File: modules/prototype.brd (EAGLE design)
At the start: 117 parts

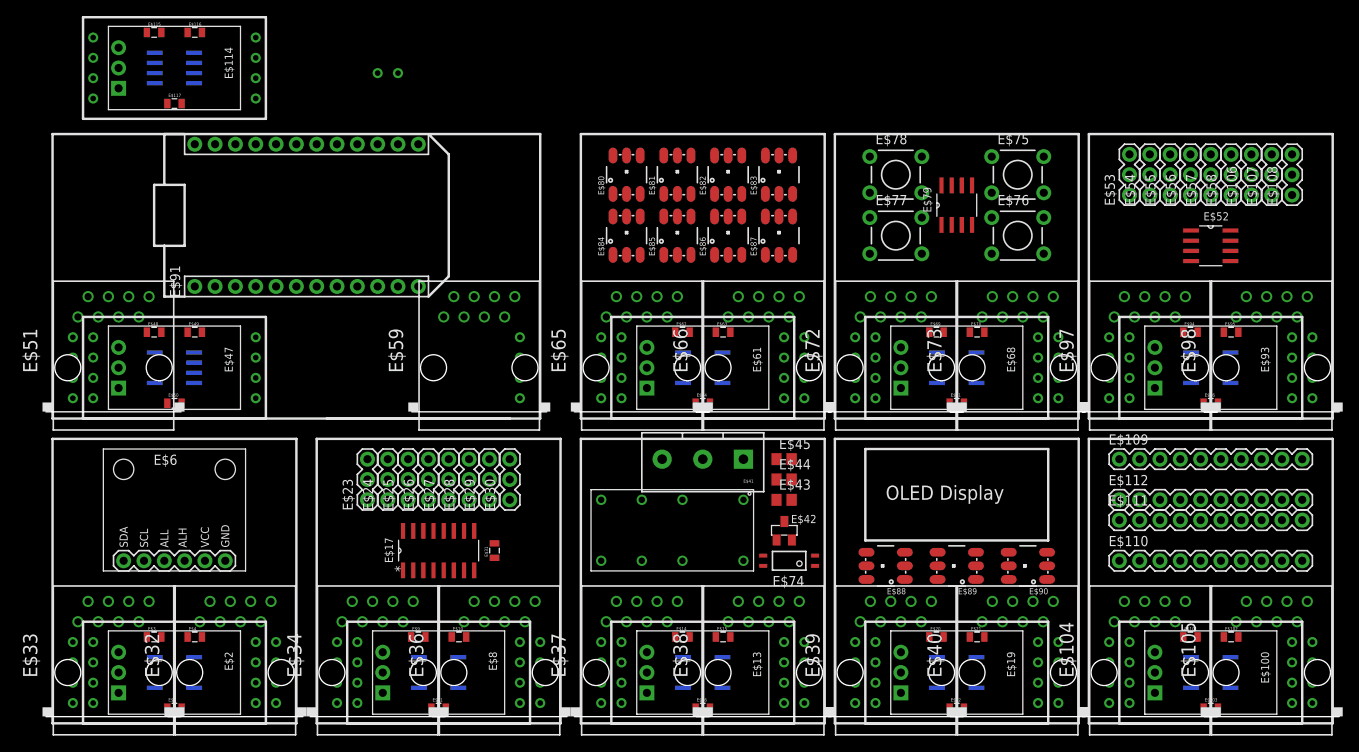
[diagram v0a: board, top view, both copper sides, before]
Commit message: Updates to v1 of reg_i2c. New ext_i2c
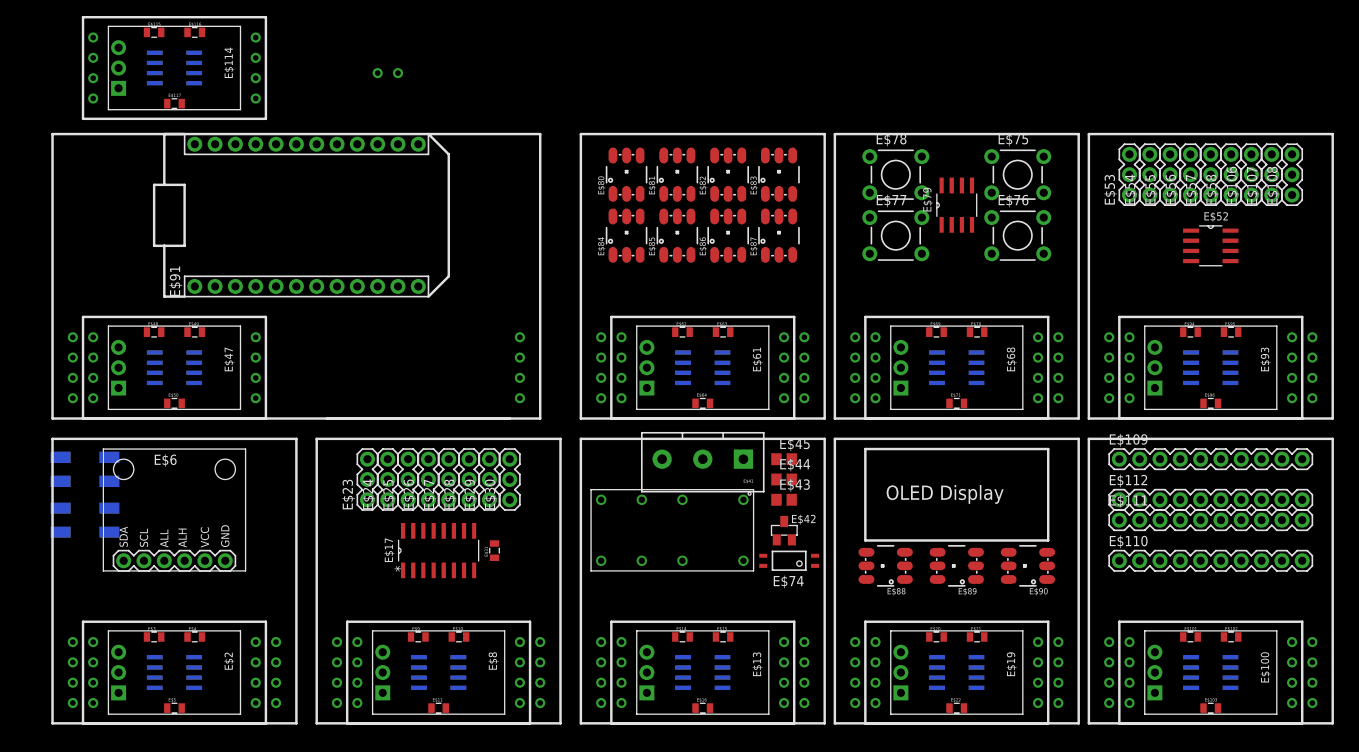
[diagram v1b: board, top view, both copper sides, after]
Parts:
- removed E$104, E$105, E$32, E$33, E$34, E$36, E$37, E$38, E$39, E$40, E$51, E$59, E$65, E$66, E$72, E$73, E$97, E$98: (no value), con-tycoelectronics:RJ45-NO-SHIELD
- added E$118, E$119: (no value), Puffin:MOLEX_MINILITE_TRAP_2
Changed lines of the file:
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@@
 <element name="E$30" library="SparkFun-Connectors" package="1X03" value="" x="57.15" y="27.94" rot="R90"/>
 <element name="E$31" library="SparkFun-Resistors" package="0805" value="" x="55.245" y="21.59" rot="R90"/>
-<element name="E$32" library="con-tycoelectronics" package="RJ45-NO-SHIELD" value="" x="22.86" y="6.35"/>
-<element name="E$33" library="con-tycoelectronics" package="RJ45-NO-SHIELD" value="" x="7.62" y="6.35"/>
-<element name="E$34" library="con-tycoelectronics" package="RJ45-NO-SHIELD" value="" x="40.64" y="6.35"/>
-<element name="E$36" library="con-tycoelectronics" package="RJ45-NO-SHIELD" value="" x="55.88" y="6.35"/>
-<element name="E$37" library="con-tycoelectronics" package="RJ45-NO-SHIELD" value="" x="73.66" y="6.35"/>
-<element name="E$38" library="con-tycoelectronics" package="RJ45-NO-SHIELD" value="" x="88.9" y="6.35"/>
-<element name="E$39" library="con-tycoelectronics" package="RJ45-NO-SHIELD" value="" x="105.41" y="6.35"/>
-<element name="E$40" library="con-tycoelectronics" package="RJ45-NO-SHIELD" value="" x="120.65" y="6.35"/>
 <element name="E$35" library="Puffin" package="DIP16-RELAY" value="" x="77.47" y="24.13" rot="R180"/>
 <element name="E$41" library="Puffin" package="SCREWTERM_0.2X3" value="" x="86.36" y="33.02" rot="R180"/>
@@
 <element name="E$49" library="SparkFun-Resistors" package="0805" value="" x="17.78" y="48.895"/>
 <element name="E$50" library="SparkFun-Resistors" package="0805" value="" x="15.24" y="40.005"/>
-<element name="E$51" library="con-tycoelectronics" package="RJ45-NO-SHIELD" value="" x="7.62" y="44.45"/>
-<element name="E$59" library="con-tycoelectronics" package="RJ45-NO-SHIELD" value="" x="53.34" y="44.45"/>
 <element name="E$60" library="Puffin" package="SOIC8" value="" x="81.28" y="44.45" rot="MR0"/>
 <element name="E$61" library="Puffin" package="MURATA_REG_HOR" value="" x="74.295" y="44.45" rot="R270"/>
@@
 <element name="E$63" library="SparkFun-Resistors" package="0805" value="" x="83.82" y="48.895"/>
 <element name="E$64" library="SparkFun-Resistors" package="0805" value="" x="81.28" y="40.005"/>
-<element name="E$65" library="con-tycoelectronics" package="RJ45-NO-SHIELD" value="" x="73.66" y="44.45"/>
-<element name="E$66" library="con-tycoelectronics" package="RJ45-NO-SHIELD" value="" x="88.9" y="44.45"/>
 <element name="E$67" library="Puffin" package="SOIC8" value="" x="113.03" y="44.45" rot="MR0"/>
 <element name="E$68" library="Puffin" package="MURATA_REG_HOR" value="" x="106.045" y="44.45" rot="R270"/>
@@
 <element name="E$70" library="SparkFun-Resistors" package="0805" value="" x="115.57" y="48.895"/>
 <element name="E$71" library="SparkFun-Resistors" package="0805" value="" x="113.03" y="40.005"/>
-<element name="E$72" library="con-tycoelectronics" package="RJ45-NO-SHIELD" value="" x="105.41" y="44.45"/>
-<element name="E$73" library="con-tycoelectronics" package="RJ45-NO-SHIELD" value="" x="120.65" y="44.45"/>
 <element name="E$74" library="optocoupler" package="MINI-FLAT-4" value="" x="92.075" y="20.32" rot="R180"/>
 <element name="E$75" library="SparkFun-Electromechanical" package="TACTILE-PTH" value="" x="120.65" y="68.58"/>
@@
 <element name="E$95" library="SparkFun-Resistors" package="0805" value="" x="147.32" y="48.895"/>
 <element name="E$96" library="SparkFun-Resistors" package="0805" value="" x="144.78" y="40.005"/>
-<element name="E$97" library="con-tycoelectronics" package="RJ45-NO-SHIELD" value="" x="137.16" y="44.45"/>
-<element name="E$98" library="con-tycoelectronics" package="RJ45-NO-SHIELD" value="" x="152.4" y="44.45"/>
 <element name="E$99" library="Puffin" package="SOIC8" value="" x="144.78" y="6.35" rot="MR0"/>
 <element name="E$100" library="Puffin" package="MURATA_REG_HOR" value="" x="137.795" y="6.35" rot="R270"/>
@@
 <element name="E$102" library="SparkFun-Resistors" package="0805" value="" x="147.32" y="10.795"/>
 <element name="E$103" library="SparkFun-Resistors" package="0805" value="" x="144.78" y="1.905"/>
-<element name="E$104" library="con-tycoelectronics" package="RJ45-NO-SHIELD" value="" x="137.16" y="6.35"/>
-<element name="E$105" library="con-tycoelectronics" package="RJ45-NO-SHIELD" value="" x="152.4" y="6.35"/>
 <element name="E$52" library="Puffin" package="SOIC8" value="" x="144.78" y="59.69"/>
 <element name="E$53" library="SparkFun-Connectors" package="1X03" value="" x="134.62" y="66.04" rot="R90"/>
@@
 <element name="E$116" library="SparkFun-Resistors" package="0805" value="" x="17.78" y="86.36"/>
 <element name="E$117" library="SparkFun-Resistors" package="0805" value="" x="15.24" y="77.47"/>
+<element name="E$118" library="Puffin" package="MOLEX_MINILITE_TRAP_2" value="" x="3.81" y="25.4" rot="MR0"/>
+<element name="E$119" library="Puffin" package="MOLEX_MINILITE_TRAP_2" value="" x="3.81" y="31.75" rot="MR0"/>
 </elements>
 <signals>
